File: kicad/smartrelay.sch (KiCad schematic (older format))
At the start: 53 parts, among them J1 OSTYK42103030, J2 OSTYK42103030, Q1 MMBT3904, Q2 2N3904, U1 TSOP38338, U2 ArduinoNano, U3 MCP16251T-I/CH

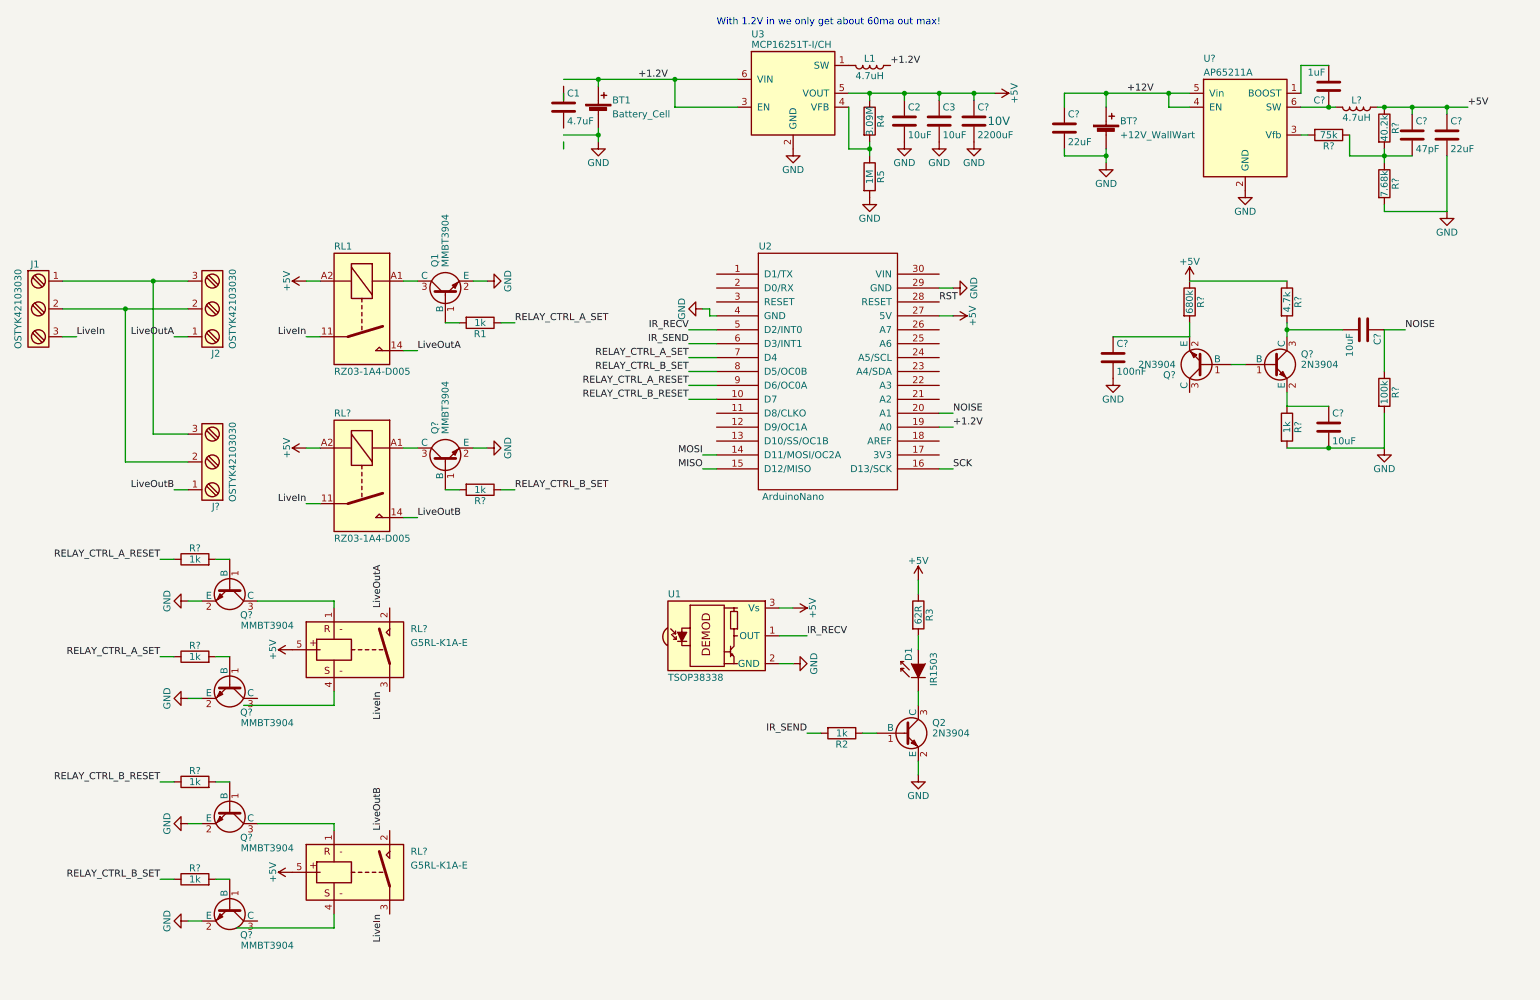
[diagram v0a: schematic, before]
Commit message: removed non-latching relays and 12V to 5V regulator from schematic
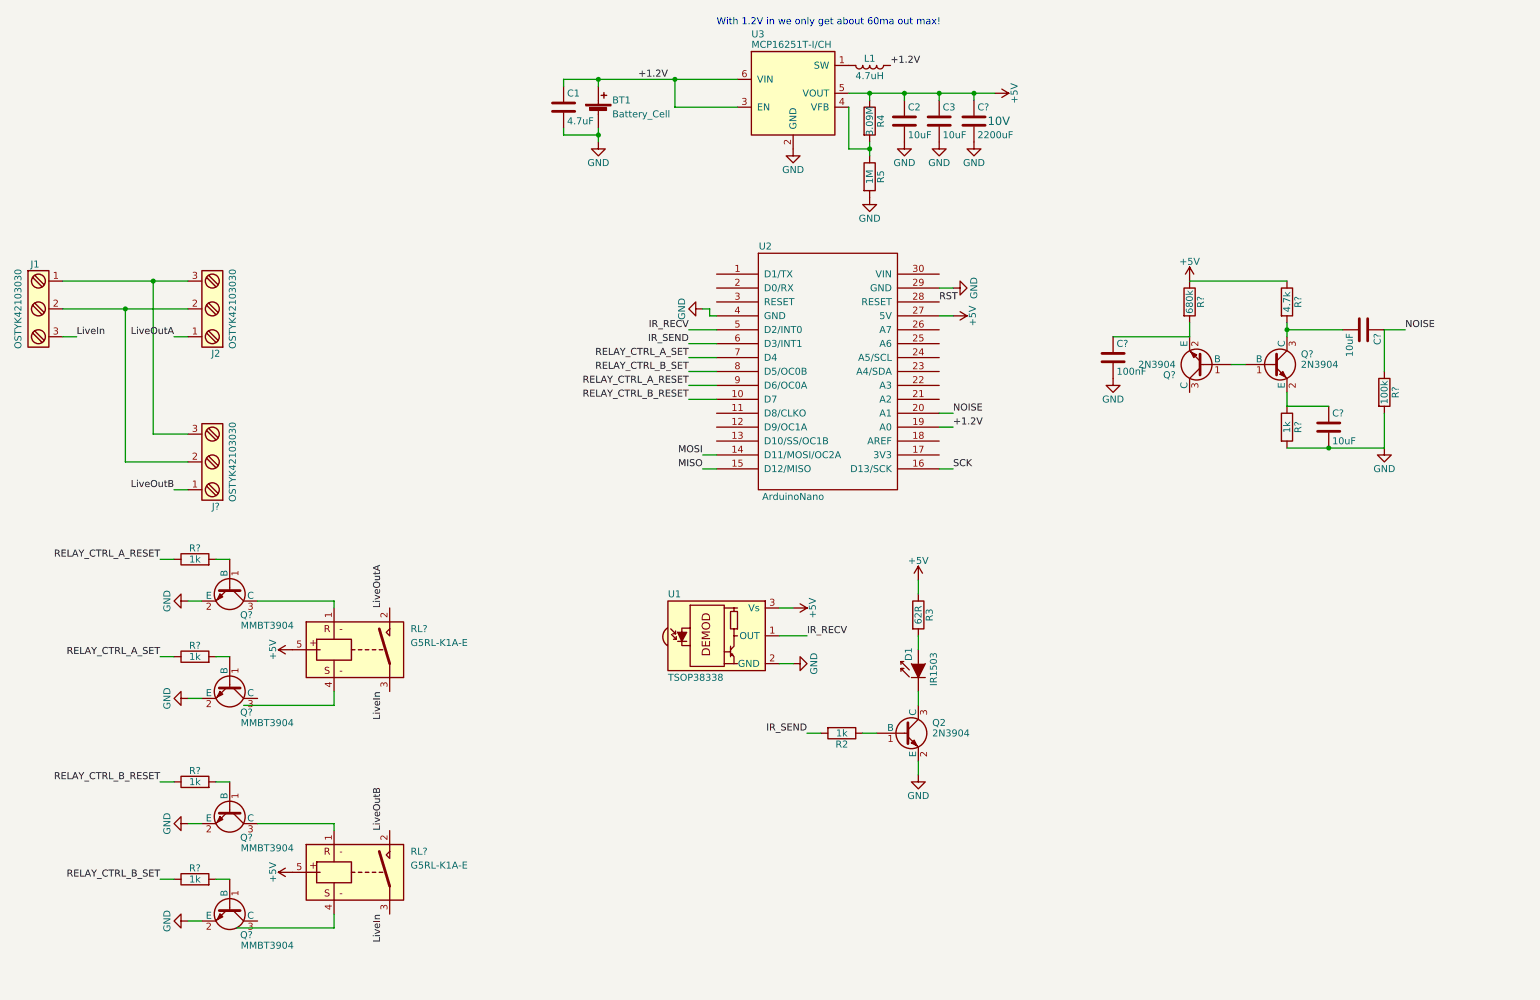
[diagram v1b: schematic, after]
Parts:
- removed BT?: +12V_WallWart, symbol Battery_Cell
- removed C? (x2): 22uF, Capacitors_THT:C_Axial_L3.8mm_D2.6mm_P7.50mm_Horizontal, symbol C
- removed C?: 1uF, Capacitors_THT:C_Axial_L3.8mm_D2.6mm_P7.50mm_Horizontal, symbol C
- removed C?: 47pF, Capacitors_THT:C_Axial_L3.8mm_D2.6mm_P7.50mm_Horizontal, symbol C
- removed L?: 4.7uH, symbol L
- removed Q1, Q?: MMBT3904, TO_SOT_Packages_SMD:SOT-23, symbol MMBT3904
- removed R1, R?: 1k, Resistors_THT:R_Axial_DIN0204_L3.6mm_D1.6mm_P5.08mm_Horizontal, symbol R
- removed R?: 40.2k, Resistors_THT:R_Axial_DIN0204_L3.6mm_D1.6mm_P5.08mm_Horizontal, symbol R
- removed R?: 7.68k, Resistors_THT:R_Axial_DIN0204_L3.6mm_D1.6mm_P5.08mm_Horizontal, symbol R
- removed R?: 75k, Resistors_THT:R_Axial_DIN0204_L3.6mm_D1.6mm_P5.08mm_Horizontal, symbol R
- removed RL1, RL?: RZ03-1A4-D005, Relays_THT:Relay_SPST_Schrack-RP-II-1-16A-FormA_RM5mm, symbol FINDER-32.21-x300
- removed U?: AP65211A, TO_SOT_Packages_SMD:SOT-23-6, symbol MCP16301
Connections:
- net labels removed: +12V
- wire segments 117 -> 82

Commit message: finished pcb, got it fabricated
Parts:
- removed J2, J?: OSTYK42103030, conn_barrier:CONN_BARRIER_STRIP_3CIRC_0.325in, symbol Screw_Terminal_1x03
- added J2, J3: CONN_01X03, Pin_Headers:Pin_Header_Straight_1x03_Pitch2.54mm, symbol CONN_01X03
- BT1: footprint (none) -> Pin_Headers:Pin_Header_Straight_1x02_Pitch2.54mm
- C1, C2, C3: footprint Capacitors_THT:C_Axial_L3.8mm_D2.6mm_P7.50mm_Horizontal -> Capacitors_THT:CP_Radial_D5.0mm_P2.50mm; symbol C -> CP1
- C4: renamed from C?; footprint Capacitors_THT:C_Axial_L3.8mm_D2.6mm_P7.50mm_Horizontal -> Capacitors_THT:CP_Radial_D10.0mm_P5.00mm; symbol C -> CP1
- C5: renamed from C?; footprint Capacitors_THT:C_Axial_L3.8mm_D2.6mm_P7.50mm_Horizontal -> Capacitors_THT:C_Disc_D4.3mm_W1.9mm_P5.00mm
- C6, C7: renamed from C?; footprint Capacitors_THT:C_Axial_L3.8mm_D2.6mm_P7.50mm_Horizontal -> Capacitors_THT:CP_Radial_D5.0mm_P2.50mm; symbol C -> CP1
- L1: footprint (none) -> Inductors_THT:L_Radial_D9.5mm_P5.00mm_Fastron_07HVP
- Q1, Q2, Q3, Q4: renamed from Q?; value MMBT3904 -> 2N3904; footprint TO_SOT_Packages_SMD:SOT-23 -> TO_SOT_Packages_THT:TO-92_Inline_Narrow_Oval; symbol MMBT3904 -> PN2222A
- Q5: renamed from Q2; footprint TO_SOT_Packages_SMD:SOT-23 -> TO_SOT_Packages_THT:TO-92_Inline_Narrow_Oval; symbol MMBT3904 -> PN2222A
- Q6, Q7: renamed from Q?; footprint TO_SOT_Packages_SMD:SOT-23 -> TO_SOT_Packages_THT:TO-92_Inline_Narrow_Oval; symbol MMBT3904 -> PN2222A
- R1, R10, R11, R12, R2, R3, R4, R9: renamed from R?; footprint Resistors_THT:R_Axial_DIN0204_L3.6mm_D1.6mm_P5.08mm_Horizontal -> Resistors_THT:R_Axial_DIN0207_L6.3mm_D2.5mm_P7.62mm_Horizontal
- R5: renamed from R2; footprint Resistors_THT:R_Axial_DIN0204_L3.6mm_D1.6mm_P5.08mm_Horizontal -> Resistors_THT:R_Axial_DIN0207_L6.3mm_D2.5mm_P7.62mm_Horizontal
- R6: renamed from R4; footprint Resistors_THT:R_Axial_DIN0204_L3.6mm_D1.6mm_P5.08mm_Horizontal -> Resistors_THT:R_Axial_DIN0207_L6.3mm_D2.5mm_P7.62mm_Horizontal
- R7: renamed from R5; footprint Resistors_THT:R_Axial_DIN0204_L3.6mm_D1.6mm_P5.08mm_Horizontal -> Resistors_THT:R_Axial_DIN0207_L6.3mm_D2.5mm_P7.62mm_Horizontal
- R8: renamed from R3; footprint Resistors_THT:R_Axial_DIN0204_L3.6mm_D1.6mm_P5.08mm_Horizontal -> Resistors_THT:R_Axial_DIN0207_L6.3mm_D2.5mm_P7.62mm_Horizontal
- RL1, RL2: renamed from RL?; footprint (none) -> LatchingRelay:LatchingRelayG5RL-K1A-E
- U3: renamed from U2; footprint (none) -> Modules:Arduino_Nano
- renumbered U3 to U2
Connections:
- net labels added: AUX1, AUX2
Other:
- moved on the sheet: J1

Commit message: smart relay redesign with smd and without arduino nano
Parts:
- removed C1: 4.7uF, Capacitors_THT:CP_Radial_D5.0mm_P2.50mm, symbol CP1
- removed C2, C3, C6, C7: 10uF, Capacitors_THT:CP_Radial_D5.0mm_P2.50mm, symbol CP1
- removed J2, J3: CONN_01X03, Pin_Headers:Pin_Header_Straight_1x03_Pitch2.54mm, symbol CONN_01X03
- removed Q1, Q2, Q3, Q4, Q5: 2N3904, TO_SOT_Packages_THT:TO-92_Inline_Narrow_Oval, symbol PN2222A
- removed R1, R2, R3, R4, R5: 1k, Resistors_THT:R_Axial_DIN0207_L6.3mm_D2.5mm_P7.62mm_Horizontal, symbol R
- removed U3: ArduinoNano, Modules:Arduino_Nano, symbol ArduinoNano
- added C1, C4, C5: 100nF, Capacitor_SMD:C_0603_1608Metric_Pad1.05x0.95mm_HandSolder, symbol device:C
- added C10, C11, C6, C7: 10uF, Capacitor_SMD:C_0805_2012Metric_Pad1.15x1.40mm_HandSolder, symbol device:C_Small
- added C2: 4.7uF, Capacitor_SMD:C_0805_2012Metric_Pad1.15x1.40mm_HandSolder, symbol device:C_Small
- added C3: 0.15nF, Capacitor_SMD:C_0603_1608Metric_Pad1.05x0.95mm_HandSolder, symbol device:C
- added D1: D_Photo, Connector_PinHeader_2.54mm:PinHeader_1x02_P2.54mm_Vertical, symbol device:D_Photo
- added J2: AVR-ISP-6, Connector_PinHeader_2.54mm:PinHeader_2x03_P2.54mm_Vertical, symbol Connector:AVR-ISP-6
- added Q1, Q2, Q3, Q4, Q5, Q6, Q8: 2N7002WT1G, Package_TO_SOT_SMD:SOT-323_SC-70_Handsoldering, symbol device:Q_NMOS_GSD
- added R1: 10k, Resistor_SMD:R_0603_1608Metric_Pad1.05x0.95mm_HandSolder, symbol device:R
- added R10: 47R, Resistor_SMD:R_0603_1608Metric_Pad1.05x0.95mm_HandSolder, symbol device:R
- added R2: 1M, Resistor_SMD:R_0603_1608Metric_Pad1.05x0.95mm_HandSolder, symbol device:R
- added R3, R4, R5, R6: 22M, Resistor_SMD:R_0603_1608Metric_Pad1.05x0.95mm_HandSolder, symbol device:R
- added R7: 470k, Resistor_SMD:R_0603_1608Metric_Pad1.05x0.95mm_HandSolder, symbol device:R
- added U1: ATMEGA328PB-AU, digikey-footprints:TQFP-32_7x7mm, symbol atmel:ATMEGA328PB-AU
- added U3: MAX918ESA, Package_SO:SOIC-8_3.9x4.9mm_P1.27mm, symbol MAX918:MAX918ESA
- BT1: footprint Pin_Headers:Pin_Header_Straight_1x02_Pitch2.54mm -> Connector_PinHeader_2.54mm:PinHeader_1x02_P2.54mm_Vertical; symbol Battery_Cell -> device:Battery_Cell
- C8: renamed from C4; footprint Capacitors_THT:CP_Radial_D10.0mm_P5.00mm -> Capacitor_THT:CP_Radial_D10.0mm_P5.00mm; symbol CP1 -> device:CP1
- C9: renamed from C5; footprint Capacitors_THT:C_Disc_D4.3mm_W1.9mm_P5.00mm -> Capacitor_SMD:C_0603_1608Metric_Pad1.05x0.95mm_HandSolder; symbol C -> device:C
- D2: renamed from D1; footprint LEDs:LED_D2.0mm_W4.8mm_H2.5mm_FlatTop -> Connector_PinHeader_2.54mm:PinHeader_1x02_P2.54mm_Vertical; symbol LD271 -> opto:LD271
- J1: symbol Screw_Terminal_1x03 -> conn:Screw_Terminal_1x03
- L1: footprint Inductors_THT:L_Radial_D9.5mm_P5.00mm_Fastron_07HVP -> Inductor_THT:L_Radial_D9.5mm_P5.00mm_Fastron_07HVP; symbol L -> device:L
- Q7: renamed from Q6; value 2N3904 -> MMBT3904; footprint TO_SOT_Packages_THT:TO-92_Inline_Narrow_Oval -> Package_TO_SOT_SMD:SOT-23_Handsoldering; symbol PN2222A -> transistors:PN2222A
- Q9: renamed from Q7; value 2N3904 -> MMBT3904; footprint TO_SOT_Packages_THT:TO-92_Inline_Narrow_Oval -> Package_TO_SOT_SMD:SOT-23_Handsoldering; symbol PN2222A -> transistors:PN2222A
- R12: renamed from R9; footprint Resistors_THT:R_Axial_DIN0207_L6.3mm_D2.5mm_P7.62mm_Horizontal -> Resistor_SMD:R_0603_1608Metric_Pad1.05x0.95mm_HandSolder; symbol R -> device:R
- R13: renamed from R8; value 62R -> 3.9R; footprint Resistors_THT:R_Axial_DIN0207_L6.3mm_D2.5mm_P7.62mm_Horizontal -> Resistor_SMD:R_0603_1608Metric_Pad1.05x0.95mm_HandSolder; symbol R -> device:R
- R14: renamed from R10; footprint Resistors_THT:R_Axial_DIN0207_L6.3mm_D2.5mm_P7.62mm_Horizontal -> Resistor_SMD:R_0603_1608Metric_Pad1.05x0.95mm_HandSolder; symbol R -> device:R
- R15: renamed from R11; footprint Resistors_THT:R_Axial_DIN0207_L6.3mm_D2.5mm_P7.62mm_Horizontal -> Resistor_SMD:R_0603_1608Metric_Pad1.05x0.95mm_HandSolder; symbol R -> device:R
- R16: renamed from R12; footprint Resistors_THT:R_Axial_DIN0207_L6.3mm_D2.5mm_P7.62mm_Horizontal -> Resistor_SMD:R_0603_1608Metric_Pad1.05x0.95mm_HandSolder; symbol R -> device:R
- R8: renamed from R6; footprint Resistors_THT:R_Axial_DIN0207_L6.3mm_D2.5mm_P7.62mm_Horizontal -> Resistor_SMD:R_0603_1608Metric_Pad1.05x0.95mm_HandSolder; symbol R -> device:R
- R9: renamed from R7; footprint Resistors_THT:R_Axial_DIN0207_L6.3mm_D2.5mm_P7.62mm_Horizontal -> Resistor_SMD:R_0603_1608Metric_Pad1.05x0.95mm_HandSolder; symbol R -> device:R
- RL1, RL2: symbol G5RL-K1A-E -> LatchingDualCoilRelay:G5RL-K1A-E
- U2: footprint TO_SOT_Packages_SMD:SOT-23-6 -> Package_TO_SOT_SMD:SOT-23-6_Handsoldering; symbol MCP1640-CH -> dc-dc:MCP1640-CH
- U4: renamed from U1; footprint Opto-Devices:IRReceiver_Vishay_MINICAST-3pin -> Connector_PinHeader_2.54mm:PinHeader_1x03_P2.54mm_Vertical; symbol TSOP382xx -> opto:TSOP382xx
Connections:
- net labels added: +5V_RELAY, CAP_ENABLE, RECV_ENABLE, WAKEUP, ~RST
- net labels removed: AUX1, AUX2, RST
- wire segments 82 -> 136
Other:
- note added: "1.4R rdsOn at 0.5A"
- note added: "1.6uA quiescent\n4mV hysteresis"
- note added: "150mA at 5V (min 3.5V?)\nfor 15ms for relays to switch\nso 33R coil resistance"
- note added: "1mA 5V draw will maybe take 8mA 1.2V draw,\nand a 2000mAh battery then last 10 days\n100uA would be 100 days\nand 25uA would be a year"
- note added: "350uA quiescent"
- note added: "5mV max offset voltage\n1mV typical"
- note added: "AVR internal pullup is 20 to 50k"
- note added: "Ceramic leakage current probably 0.5uA max"
- note added: "For 0.5A bursts w/ 2.2V forward voltage"
- note added: "Noise generation circuit"
- note added: "Quiescent current, 4uA output"
- note added: "We'll have to take around 300ms\nto charge before we can drive the relay"
- note added: "With 1.2V in we only get about 60mA out max!\n\n"
- note added: "less than 1uA in power down mode"
- note added: "max 1.6R rdsOn"
- note added: "max 110uA leakage,\n22uA for low leakage nichicon"
- note removed: "With 1.2V in we only get about 60ma out max!\n\n"
- moved on the sheet: D2, J1, R13, U4
